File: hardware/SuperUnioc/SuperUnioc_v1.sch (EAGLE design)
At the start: 57 parts, among them IC1 MAX3232CSE, IC5 XMEGA128-A1

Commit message: super unioc: add GP2 connector
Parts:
- added C10, C11, C12, C13: 10UFC, robotter_capacitor:10UFC
- added GP2: MICROMATCH-12_SMD, robotter_connector:MICROMATCH-12_SMD
- added R2, R3, R4, R5: 270-F, robotter_resistor:270-F
- added R6, R7, R8, R9: (no value), robotter_resistor:470-F
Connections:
- removed net ASD0: IC5.PB7(ADCB7/AC0-OUT/TDO)
- removed net CONF_DONE: IC5.PB0(ADCB0/AREFB)
- removed net DATA0: IC5.PB4(ADCB4/TMS)
- removed net DCLK: IC5.PB3(ADCB3/DAC1)
- removed net FPGA_IRQ_3V3: IC5.PB5(ADCB5/TDI)
- removed net NCE: IC5.PB2(ADCB2/DAC0)
- removed net NCONFIG: IC5.PB1(ADCB1)
- removed net NCS0: IC5.PB6(ADCB6/TCK)
- new net GP2_0_0-1V: IC5.PB3(ADCB3/DAC1), R5.2, R9.1
- new net GP2_1_0-1V: IC5.PB2(ADCB2/DAC0), R2.2, R6.1
- new net GP2_2_0-1V: IC5.PB1(ADCB1), R4.2, R8.1
- new net GP2_3_0-1V: IC5.PB0(ADCB0/AREFB), R3.2, R7.1
- new net N$22: GP2-1.S, R9.2
- new net N$24: GP2-7.S, R8.2
- new net N$36: GP2-10.S, R7.2
- new net N$37: GP2-4.S, R6.2
- net +3V3: no longer R21.2, R23.2
- net +5V: now also C10.1, C11.1, C12.1, C13.1, GP2-12.S, GP2-3.S, GP2-6.S, GP2-9.S
- net GND: now also C10.2, C11.2, C12.2, C13.2, GP2-11.S, GP2-2.S, GP2-5.S, GP2-8.S, R2.1, R21.2, R23.2, R3.1, R4.1, R5.1
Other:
- note added: "que la nappe ait juste a etre splittée en 4"
- note added: "verifier pinout du gp2"
- note removed: "verifier pinout connecteur"
- moved on the sheet: R21, R23

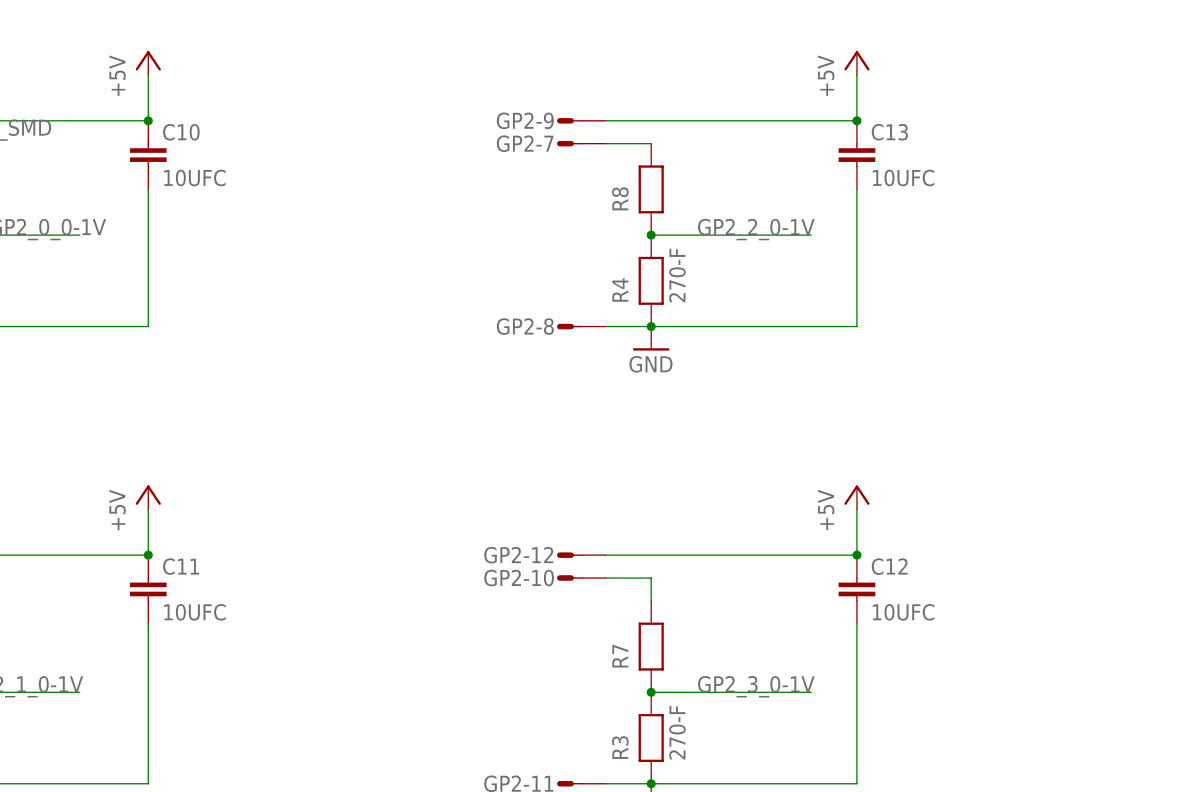
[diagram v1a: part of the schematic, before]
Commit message: radiospares part number added
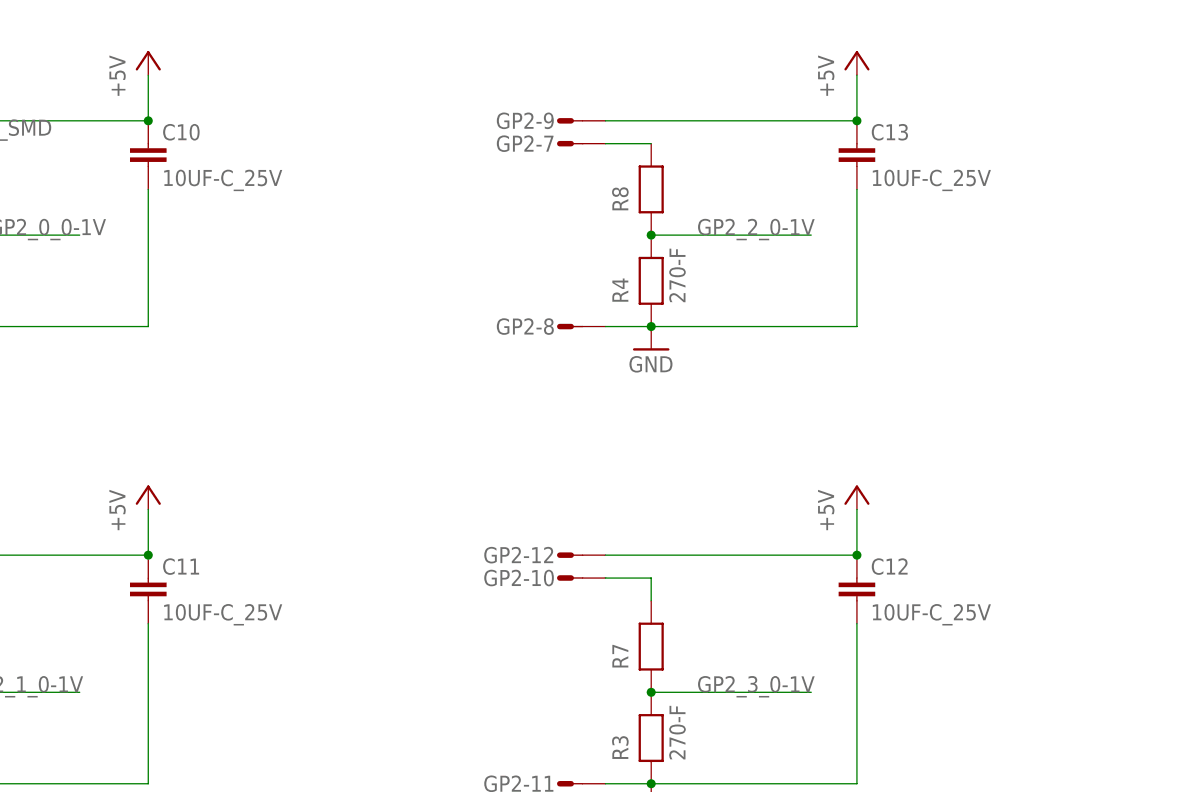
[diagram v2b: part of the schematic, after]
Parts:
- C10, C11, C12, C13: value 10UFC -> 10UF-C_25V; device robotter_capacitor:10UFC -> robotter_capacitor:10UF-C_25V
- C2, C7, C8: device robotter_capacitor:C_1UF -> robotter_capacitor:1UFD_25V
- D1: device robotter_ic:MMSD4148 -> robotter_ic:MMSD4148'
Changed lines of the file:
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@@
 <?xml version="1.0" encoding="utf-8"?>
 <!DOCTYPE eagle SYSTEM "eagle.dtd">
-<eagle version="6.4">
+<eagle version="6.5.0">
 <drawing>
 <settings>
@@
 <part name="GND10" library="supply1" deviceset="GND" device=""/>
 <part name="GND11" library="supply1" deviceset="GND" device=""/>
-<part name="C2" library="robotter_capacitor" deviceset="C_" device="1UF" value="1UF_50V_1206"/>
-<part name="C7" library="robotter_capacitor" deviceset="C_" device="1UF" value="1UF_50V_1206"/>
-<part name="C8" library="robotter_capacitor" deviceset="C_" device="1UF" value="1UF_50V_1206"/>
+<part name="C2" library="robotter_capacitor" deviceset="1UF" device="D_25V" value="1UF_50V_1206"/>
+<part name="C7" library="robotter_capacitor" deviceset="1UF" device="D_25V" value="1UF_50V_1206"/>
+<part name="C8" library="robotter_capacitor" deviceset="1UF" device="D_25V" value="1UF_50V_1206"/>
 <part name="C9" library="robotter_capacitor" deviceset="100NF" device="-F" value="100nF_0603_50V"/>
-<part name="D1" library="robotter_ic" deviceset="MMSD4148" device="" value="MMSD4148"/>
+<part name="D1" library="robotter_ic" deviceset="MMSD4148" device="'" value="MMSD4148"/>
 <part name="R1" library="robotter_resistor" deviceset="10K" device="-F"/>
 <part name="L1" library="robotter_inductor" deviceset="NPIS64D" device="471MTRF"/>
@@
 <part name="GND14" library="supply1" deviceset="GND" device=""/>
 <part name="GND15" library="supply1" deviceset="GND" device=""/>
-<part name="C10" library="robotter_capacitor" deviceset="10UF" device="C"/>
-<part name="C11" library="robotter_capacitor" deviceset="10UF" device="C"/>
-<part name="C12" library="robotter_capacitor" deviceset="10UF" device="C"/>
-<part name="C13" library="robotter_capacitor" deviceset="10UF" device="C"/>
+<part name="C10" library="robotter_capacitor" deviceset="10UF" device="-C_25V"/>
+<part name="C11" library="robotter_capacitor" deviceset="10UF" device="-C_25V"/>
+<part name="C12" library="robotter_capacitor" deviceset="10UF" device="-C_25V"/>
+<part name="C13" library="robotter_capacitor" deviceset="10UF" device="-C_25V"/>
 <part name="GND9" library="supply1" deviceset="GND" device=""/>
 </parts>

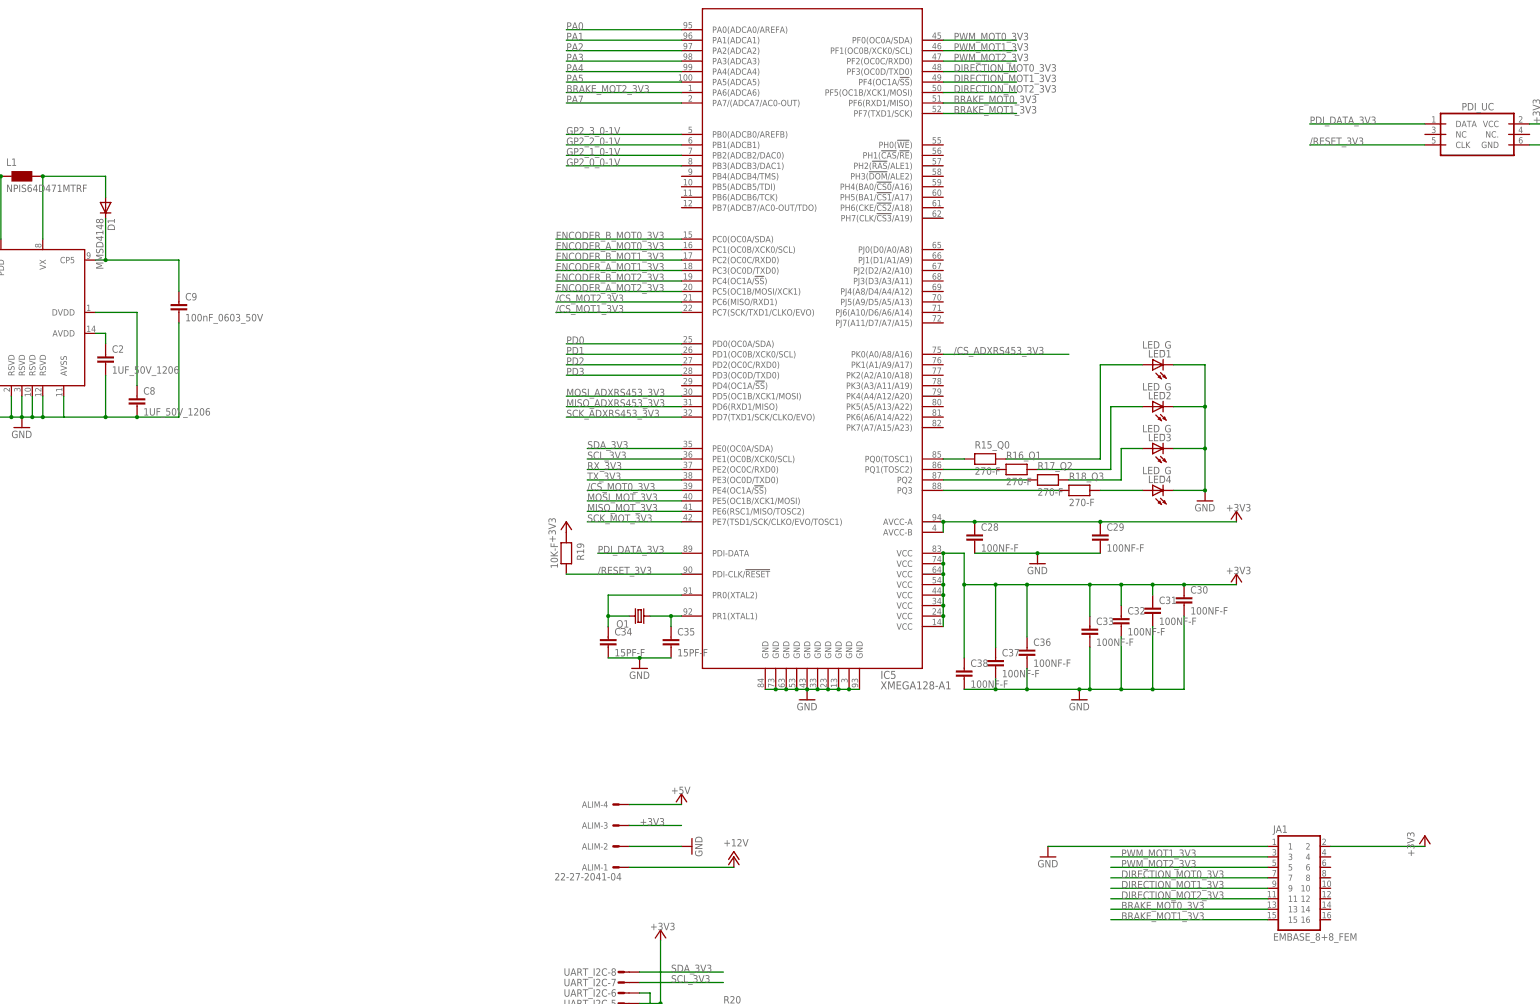
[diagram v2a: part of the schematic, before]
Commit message: ferrit bead on avcc added
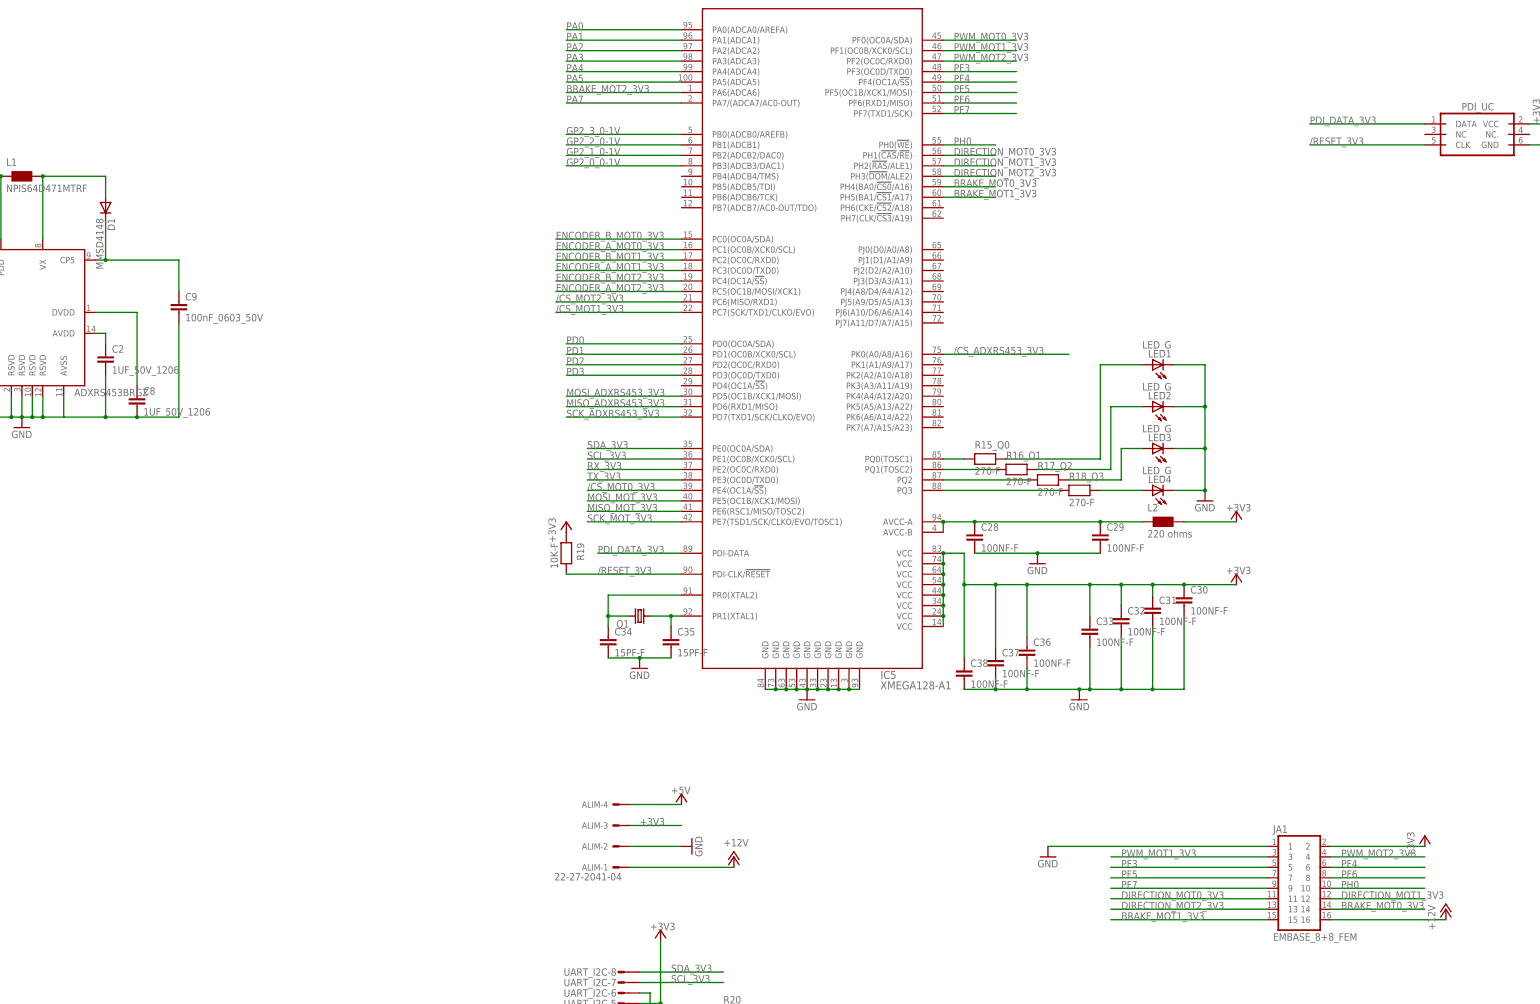
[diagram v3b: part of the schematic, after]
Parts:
- added L2: 220 ohms, robotter_inductor:FERRITE_220OHMS
- IC2: value (none) -> ADXRS453BRGZ
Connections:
- new net N$25: C28.1, C29.1, IC5.AVCC-A, IC5.AVCC-B, L2.1
- new net PF3: IC5.PF3(OC0D/TXD0), JA1.5
- new net PF4: IC5.PF4(OC1A/!SS!), JA1.6
- new net PF5: IC5.PF5(OC1B/XCK1/MOSI), JA1.7
- new net PF6: IC5.PF6(RXD1/MISO), JA1.8
- new net PF7: IC5.PF7(TXD1/SCK), JA1.9
- new net PH0: IC5.PH0(!WE!), JA1.10
- net +12V: now also JA1.16
- net +3V3: now also L2.2; no longer C28.1, C29.1, IC5.AVCC-A, IC5.AVCC-B
- net BRAKE_MOT0_3V3: now also IC5.PH4(BA0/!CS0!/A16), JA1.14; no longer IC5.PF6(RXD1/MISO), JA1.13
- net BRAKE_MOT1_3V3: now also IC5.PH5(BA1/!CS1!/A17); no longer IC5.PF7(TXD1/SCK)
- net DIRECTION_MOT0_3V3: now also IC5.PH1(!CAS!/!RE!), JA1.11; no longer IC5.PF3(OC0D/TXD0), JA1.7
- net DIRECTION_MOT1_3V3: now also IC5.PH2(!RAS!/ALE1), JA1.12; no longer IC5.PF4(OC1A/!SS!), JA1.9
- net DIRECTION_MOT2_3V3: now also IC5.PH3(!DOM!/ALE2), JA1.13; no longer IC5.PF5(OC1B/XCK1/MOSI), JA1.11
- net PWM_MOT2_3V3: now also JA1.4; no longer JA1.5

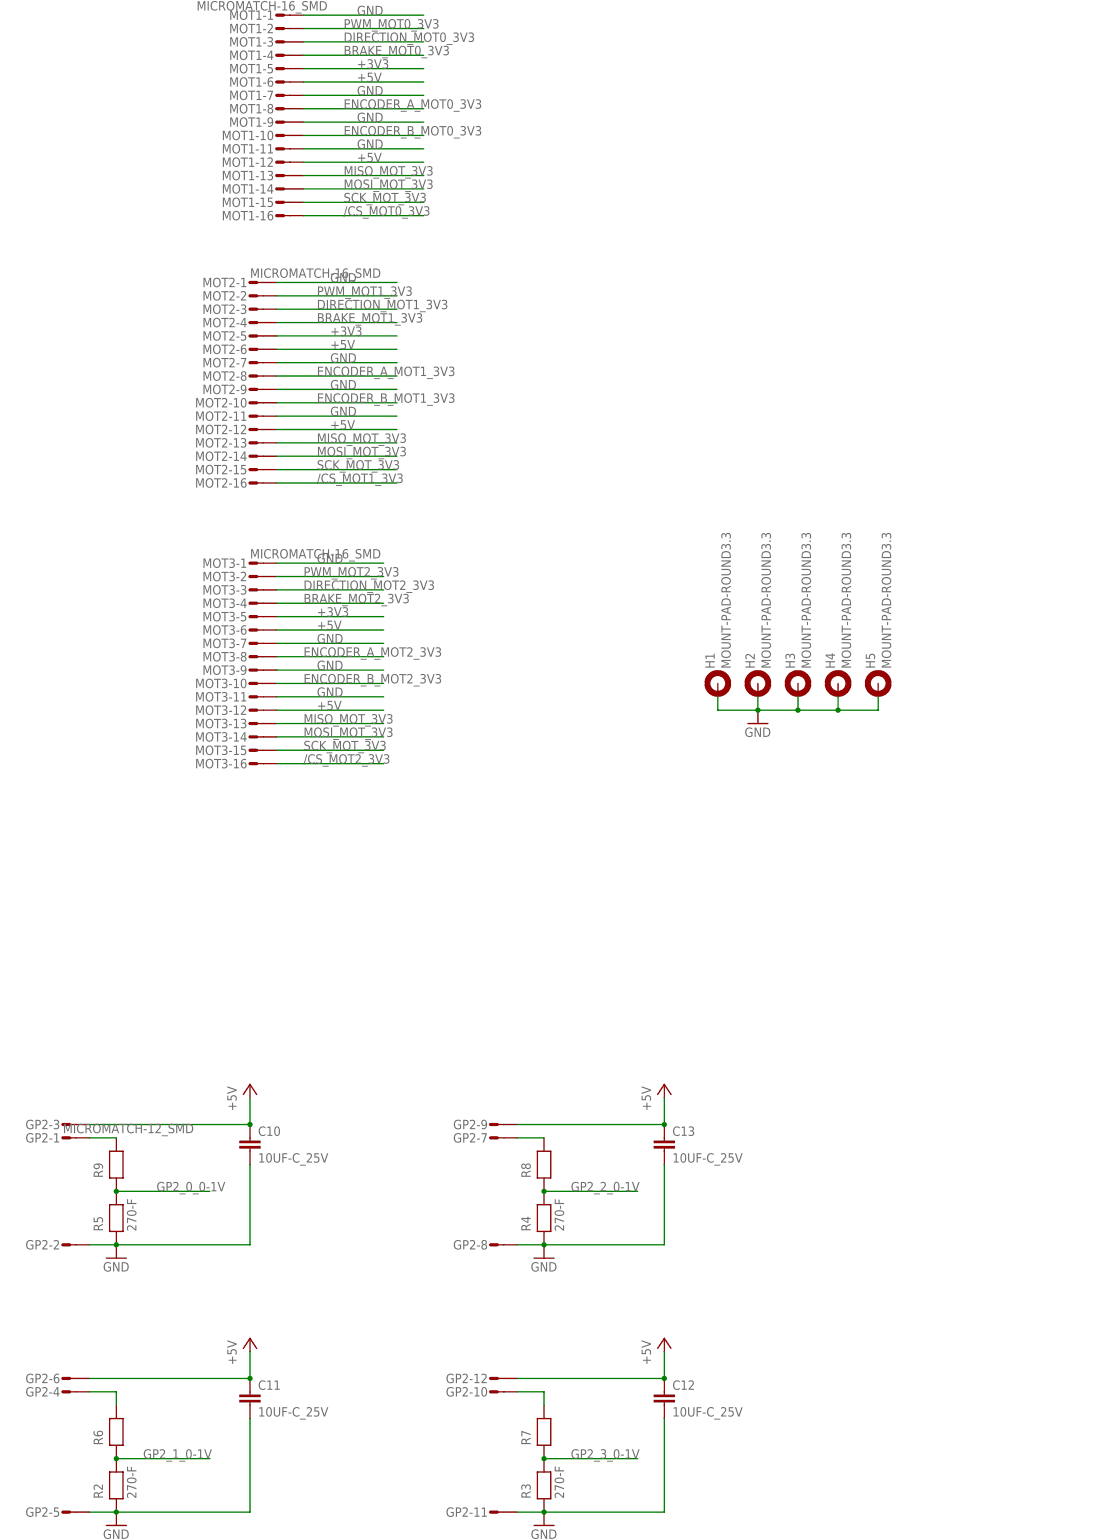
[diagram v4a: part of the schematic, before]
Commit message: SuperUnioc/SuperUnioc_v1.brd
mouser ref added
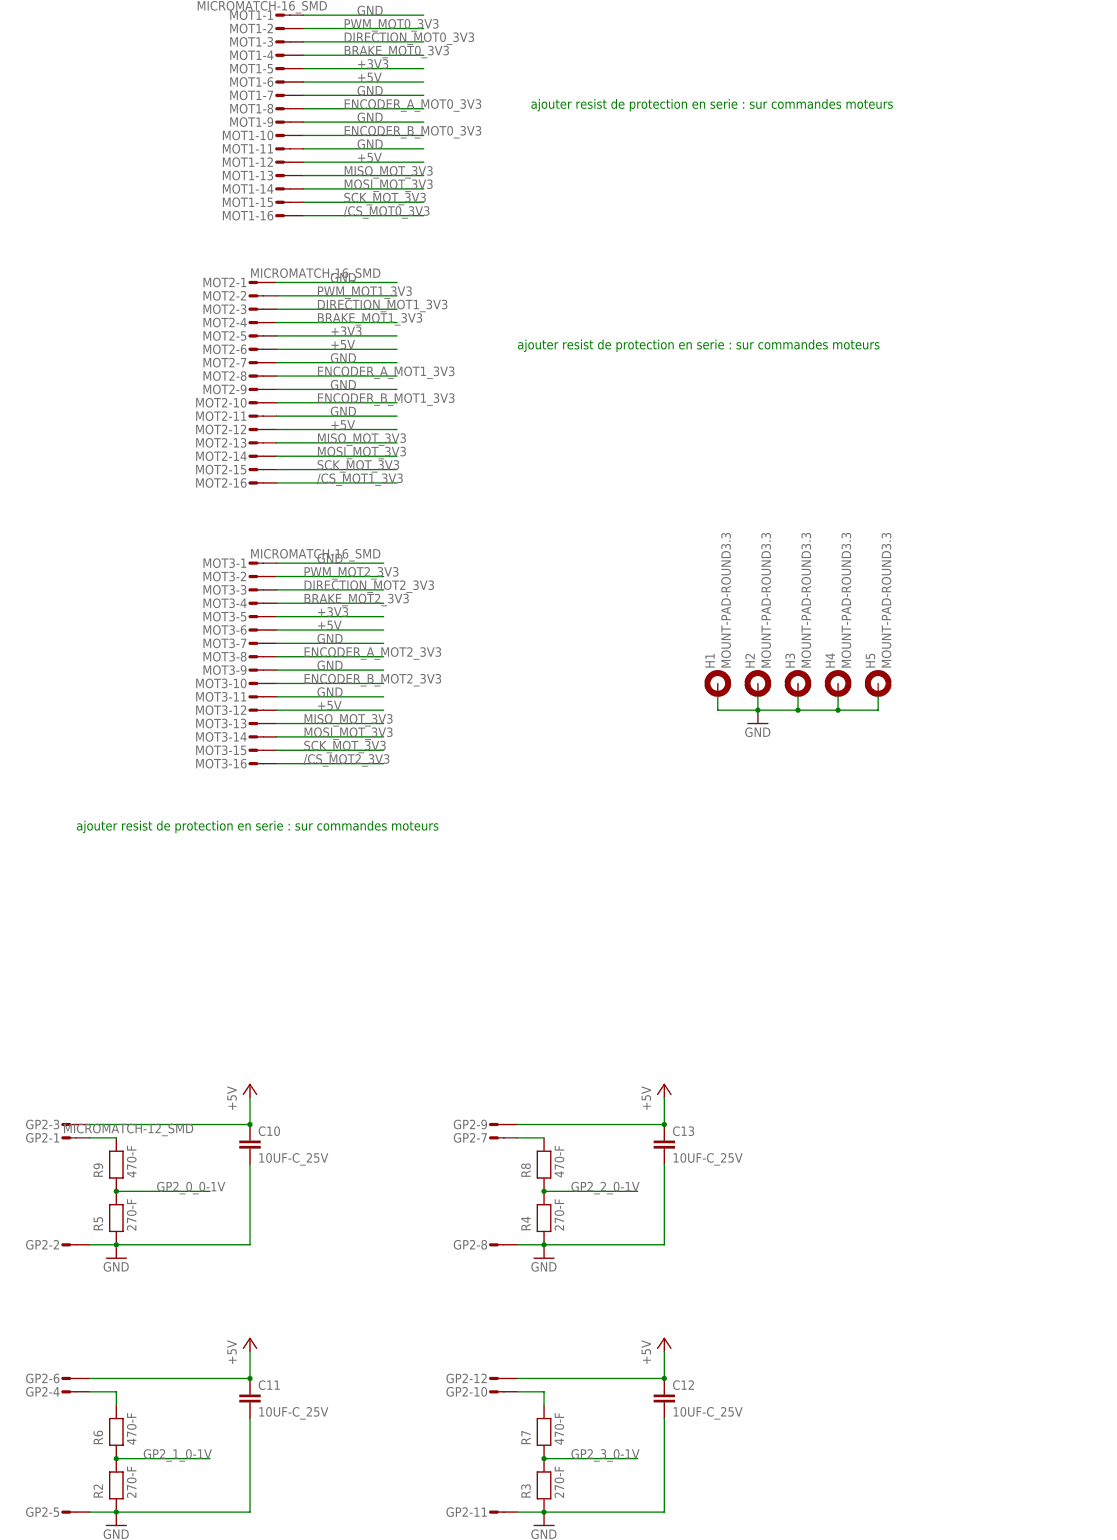
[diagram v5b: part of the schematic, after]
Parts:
- R6, R7, R8, R9: value (none) -> 470-F
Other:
- note added: "ajouter resist de protection en serie : sur commandes moteurs"
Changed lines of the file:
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@@
 <text x="25.4" y="-134.62" size="1.778" layer="91">verifier pinout du gp2</text>
 <text x="60.96" y="-134.62" size="1.778" layer="91">que la nappe ait juste a etre splittée en 4</text>
+<text x="35.56" y="15.24" size="1.778" layer="91">ajouter resist de protection en serie : sur commandes moteurs </text>
+<text x="121.92" y="152.4" size="1.778" layer="91">ajouter resist de protection en serie : sur commandes moteurs </text>
+<text x="119.38" y="106.68" size="1.778" layer="91">ajouter resist de protection en serie : sur commandes moteurs </text>
 </plain>
 <instances>
